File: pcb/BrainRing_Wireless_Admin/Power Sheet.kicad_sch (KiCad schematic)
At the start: 23 parts, among them J2 USB_C_Receptacle_PowerOnly_6P, SW1 SS12D11G5, U4 IP5305, U5 AMS1117-3.3

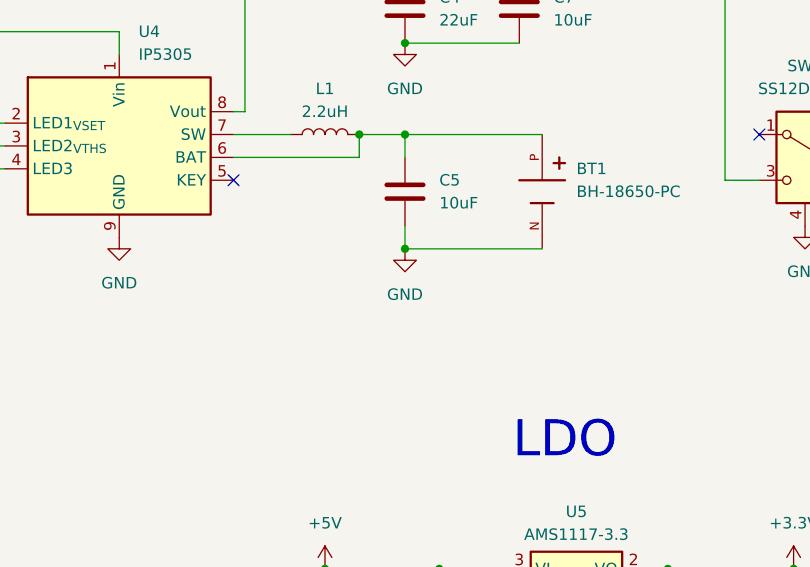
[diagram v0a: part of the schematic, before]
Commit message: Refactor firmware: fair first-press detection, single player firmware, animations
- Shared protocol/radio config (include/brainring.h) and non-blocking melody player (include/melody.h)
- Admin: timestamp-based winner resolution with 30 ms decision window, reject pre-reset presses,
  fresh ACK payloads, press/reset sound and LED indication, idle breathing
- Players: one firmware for all boards, ID/color stored in EEPROM with on-device color menu,
  reliable press delivery with per-ID retry delays, link-loss detection,
  strip + button LED (PWM) animations, 3 random win melodies and a lose melody
- Admin case generator, print files and PCB updates

Co-Authored-By: Claude Opus 5.5 <noreply@anthropic.com>
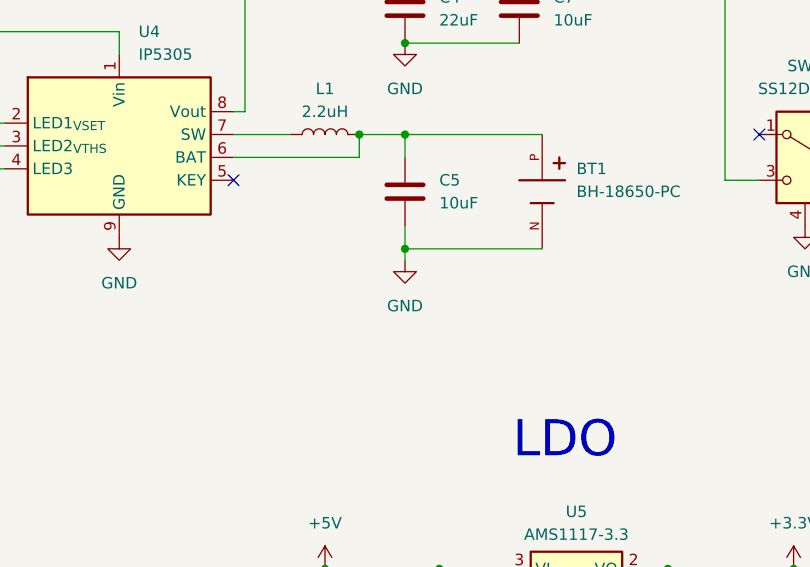
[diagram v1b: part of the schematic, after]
